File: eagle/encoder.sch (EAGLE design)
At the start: 22 parts, among them IC1 LM339D, J1 SPI, U1 MCP42XXX, U2 ATMEGA328P

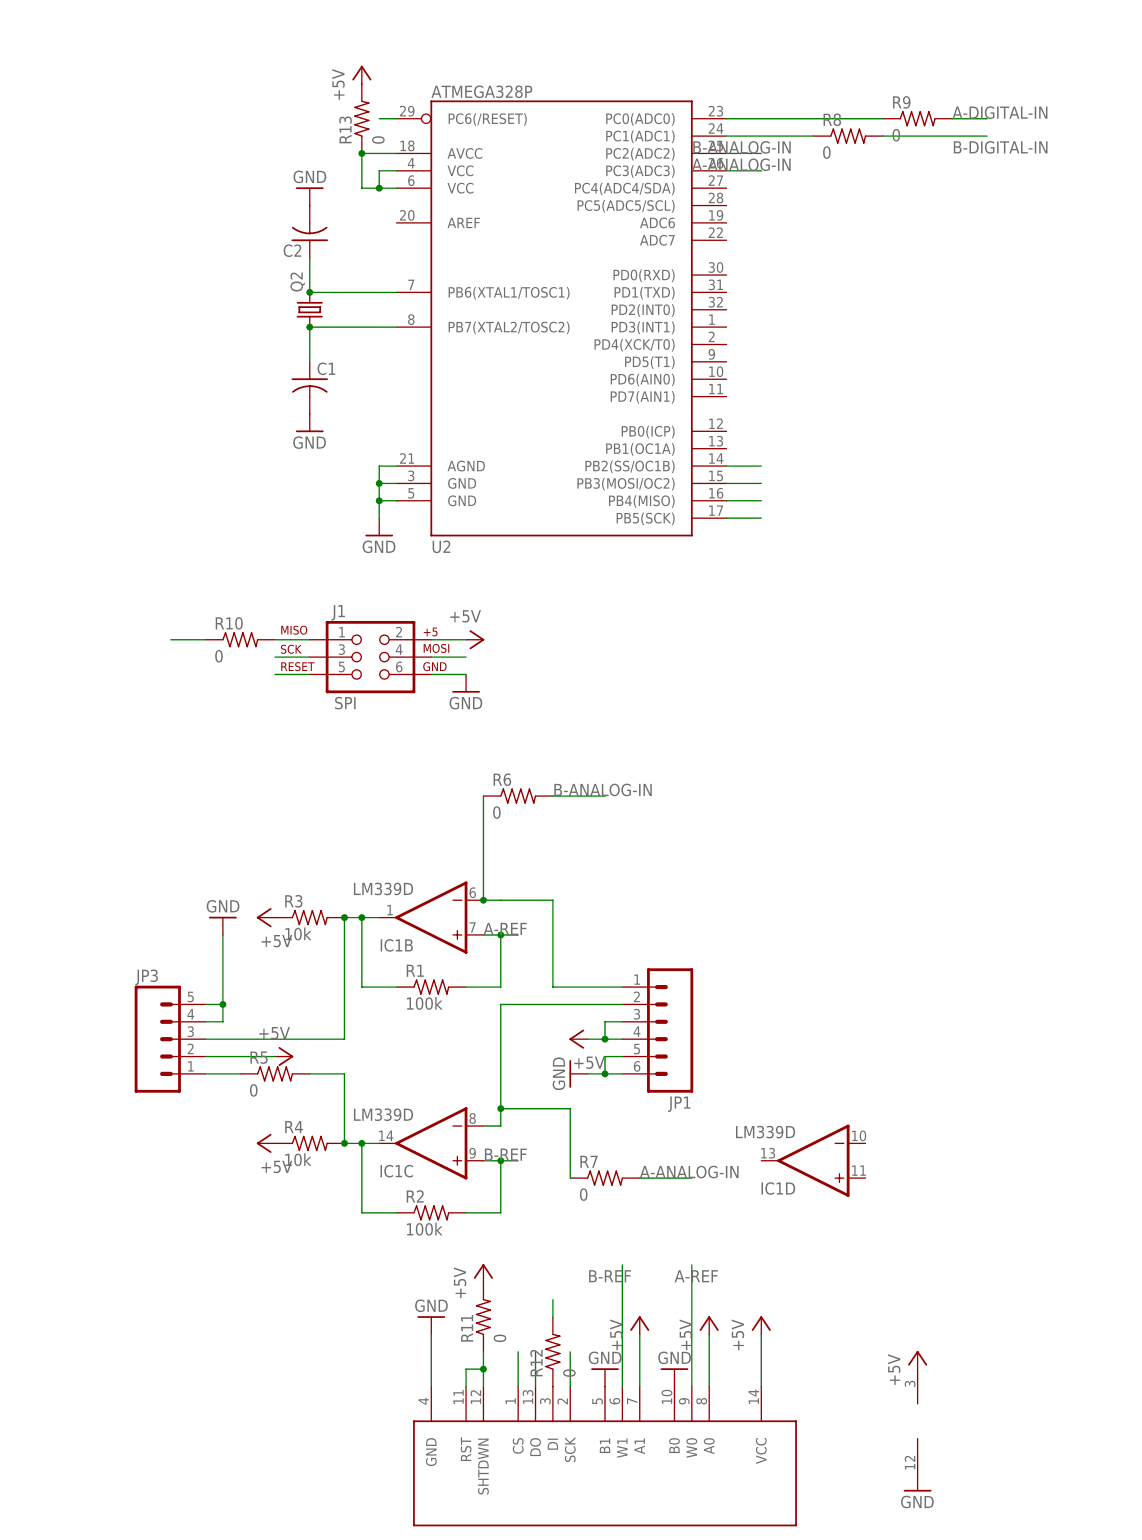
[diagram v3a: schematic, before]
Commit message: Added I2C and power connections.
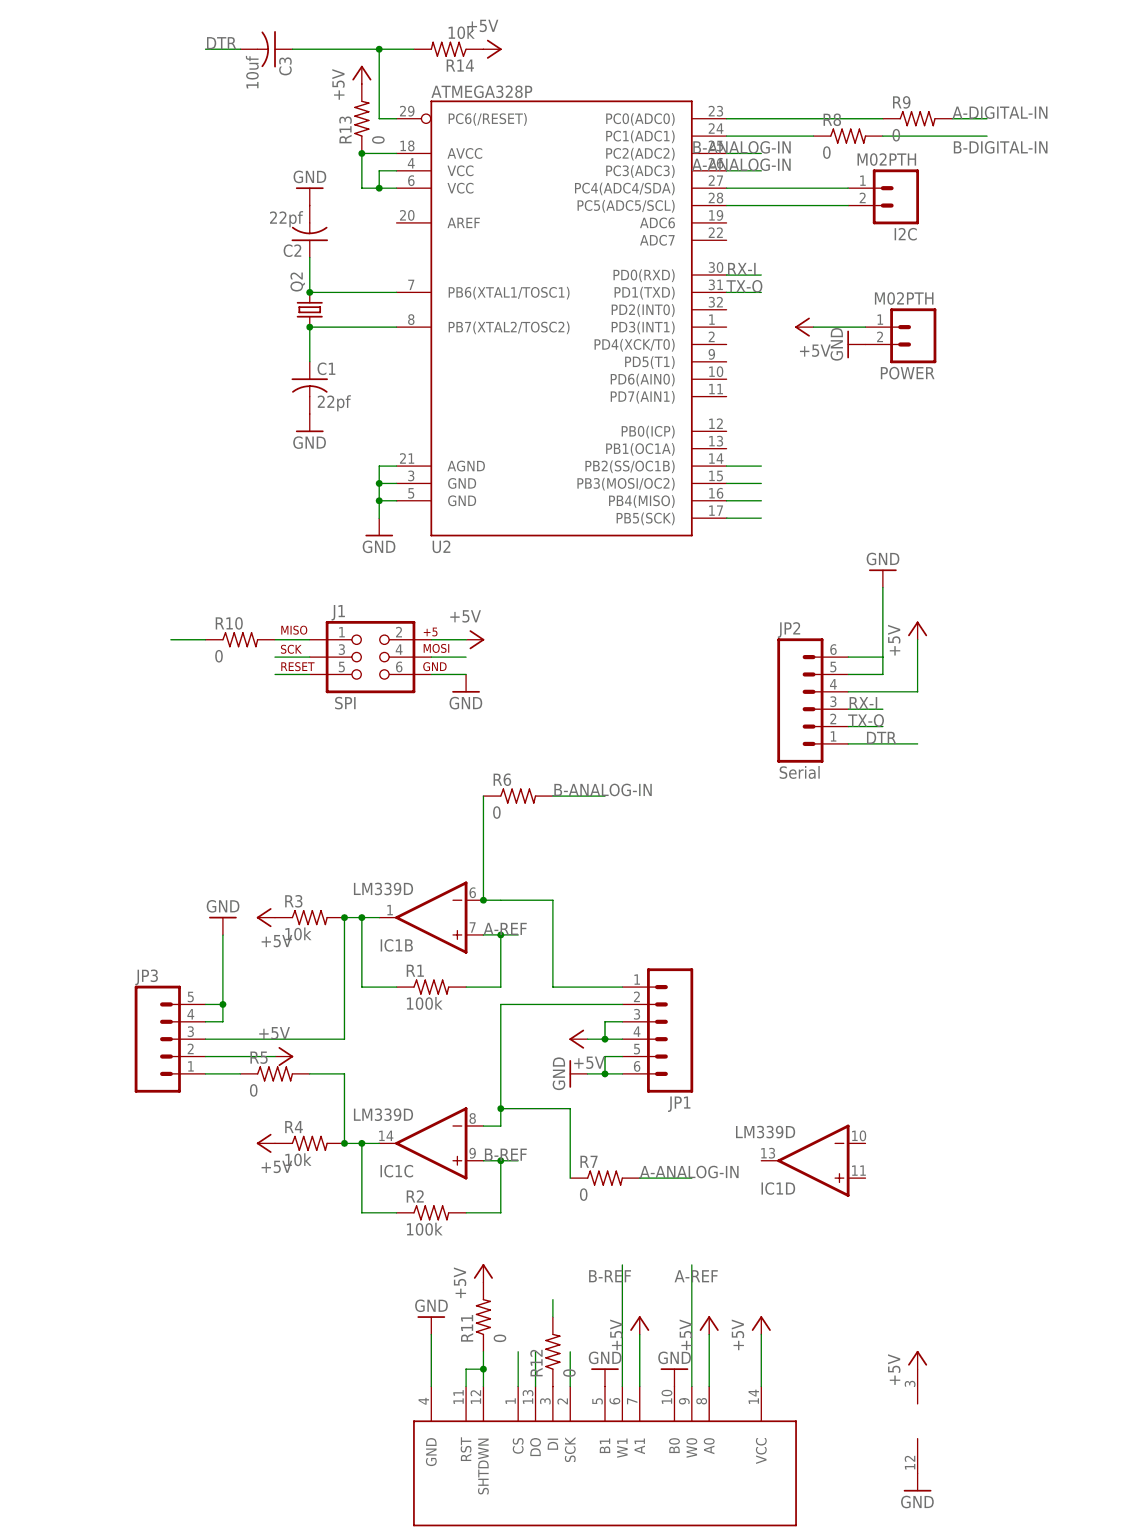
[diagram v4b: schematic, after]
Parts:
- added C3: 10uf, resistor:C-USC1206
- added I2C, POWER: M02PTH, SparkFun-Connectors:M02PTH
- added JP2: Serial, SparkFun-Connectors:M06SIP
- added R14: 10k, resistor:R-US_R1206
- C1, C2: value (none) -> 22pf
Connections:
- new net DTR: C3.2, JP2.1
- new net N$12: I2C.1, U2.PC4(ADC4/SDA)
- new net N$13: I2C.2, U2.PC5(ADC5/SCL)
- new net RX-I: JP2.3, U2.PD0(RXD)
- new net TX-O: JP2.2, U2.PD1(TXD)
- net +5V: now also JP2.4, POWER.1, R14.1
- net GND: now also JP2.5, JP2.6, POWER.2
- net RESET: now also C3.1, R14.2
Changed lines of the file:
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@@
 <part name="P+12" library="supply1" deviceset="+5V" device=""/>
 <part name="Q2" library="crystal" deviceset="CRYSTAL" device="HC49UP"/>
-<part name="C1" library="resistor" deviceset="C-US" device="C1206"/>
-<part name="C2" library="resistor" deviceset="C-US" device="C1206"/>
+<part name="C1" library="resistor" deviceset="C-US" device="C1206" value="22pf"/>
+<part name="C2" library="resistor" deviceset="C-US" device="C1206" value="22pf"/>
 <part name="GND9" library="supply1" deviceset="GND" device=""/>
 <part name="GND10" library="supply1" deviceset="GND" device=""/>
+<part name="R14" library="resistor" deviceset="R-US_" device="R1206" value="10k"/>
+<part name="P+9" library="supply1" deviceset="+5V" device=""/>
+<part name="C3" library="resistor" deviceset="C-US" device="C1206" value="10uf"/>
+<part name="JP2" library="SparkFun-Connectors" deviceset="M06" device="SIP" value="Serial"/>
+<part name="GND11" library="supply1" deviceset="GND" device=""/>
+<part name="P+13" library="supply1" deviceset="+5V" device=""/>
+<part name="I2C" library="SparkFun-Connectors" deviceset="M02" device="PTH"/>
+<part name="POWER" library="SparkFun-Connectors" deviceset="M02" device="PTH"/>
+<part name="P+14" library="supply1" deviceset="+5V" device=""/>
+<part name="GND12" library="supply1" deviceset="GND" device=""/>
 </parts>
 <sheets>
@@
 <instance part="GND9" gate="1" x="35.56" y="165.1"/>
 <instance part="GND10" gate="1" x="35.56" y="200.66" rot="R180"/>
+<instance part="R14" gate="G$1" x="55.88" y="220.98" rot="R180"/>
+<instance part="P+9" gate="1" x="63.5" y="220.98" rot="R270"/>
+<instance part="C3" gate="G$1" x="30.48" y="220.98" rot="R270"/>
+<instance part="JP2" gate="G$1" x="109.22" y="124.46"/>
+<instance part="GND11" gate="1" x="119.38" y="144.78" rot="R180"/>
+<instance part="P+13" gate="1" x="124.46" y="137.16"/>
+<instance part="I2C" gate="G$1" x="121.92" y="200.66" rot="R180"/>
+<instance part="POWER" gate="G$1" x="124.46" y="180.34" rot="R180"/>
+<instance part="P+14" gate="1" x="106.68" y="180.34" rot="R90"/>
+<instance part="GND12" gate="1" x="114.3" y="177.8" rot="R270"/>
 </instances>
 <busses>
@@
 <pinref part="P+12" gate="1" pin="+5V"/>
 </segment>
+<segment>
+<pinref part="R14" gate="G$1" pin="1"/>
+<pinref part="P+9" gate="1" pin="+5V"/>
+</segment>
+<segment>
+<pinref part="JP2" gate="G$1" pin="4"/>
+<wire x1="114.3" y1="127" x2="124.46" y2="127" width="0.1524" layer="91"/>
+<wire x1="124.46" y1="127" x2="124.46" y2="134.62" width="0.1524" layer="91"/>
+<pinref part="P+13" gate="1" pin="+5V"/>
+</segment>
+<segment>
+<pinref part="POWER" gate="G$1" pin="1"/>
+<pinref part="P+14" gate="1" pin="+5V"/>
+<wire x1="109.22" y1="180.34" x2="116.84" y2="180.34" width="0.1524" layer="91"/>
+</segment>
 </net>
 <net name="GND" class="0">
@@
 <pinref part="GND10" gate="1" pin="GND"/>
 </segment>
+<segment>
+<pinref part="JP2" gate="G$1" pin="5"/>
+<wire x1="114.3" y1="129.54" x2="119.38" y2="129.54" width="0.1524" layer="91"/>
+<wire x1="119.38" y1="129.54" x2="119.38" y2="132.08" width="0.1524" layer="91"/>
+<pinref part="JP2" gate="G$1" pin="6"/>
+<wire x1="119.38" y1="132.08" x2="119.38" y2="142.24" width="0.1524" layer="91"/>
+<wire x1="114.3" y1="132.08" x2="119.38" y2="132.08" width="0.1524" layer="91"/>
+<pinref part="GND11" gate="1" pin="GND"/>
+</segment>
+<segment>
+<pinref part="POWER" gate="G$1" pin="2"/>
+<pinref part="GND12" gate="1" pin="GND"/>
+</segment>
 </net>
 <net name="B-REF" class="0">
@@
 <pinref part="U2" gate="G$1" pin="PC6(/RESET)"/>
 <wire x1="48.26" y1="210.82" x2="45.72" y2="210.82" width="0.1524" layer="91"/>
+<wire x1="45.72" y1="210.82" x2="45.72" y2="220.98" width="0.1524" layer="91"/>
+<wire x1="45.72" y1="220.98" x2="50.8" y2="220.98" width="0.1524" layer="91"/>
+<pinref part="R14" gate="G$1" pin="2"/>
+<wire x1="45.72" y1="220.98" x2="33.02" y2="220.98" width="0.1524" layer="91"/>
+<pinref part="C3" gate="G$1" pin="1"/>
+<junction x="45.72" y="220.98"/>
 </segment>
 <segment>
@@
 </segment>
 </net>
+<net name="DTR" class="0">
+<segment>
+<pinref part="C3" gate="G$1" pin="2"/>
+<wire x1="25.4" y1="220.98" x2="20.32" y2="220.98" width="0.1524" layer="91"/>
+<label x="20.32" y="220.98" size="1.778" layer="95"/>
+</segment>
+<segment>
+<wire x1="114.3" y1="119.38" x2="124.46" y2="119.38" width="0.1524" layer="91"/>
+<label x="116.84" y="119.38" size="1.778" layer="95"/>
+<pinref part="JP2" gate="G$1" pin="1"/>
+</segment>
+</net>
+<net name="RX-I" class="0">
+<segment>
+<pinref part="U2" gate="G$1" pin="PD0(RXD)"/>
+<wire x1="96.52" y1="187.96" x2="101.6" y2="187.96" width="0.1524" layer="91"/>
+<label x="96.52" y="187.96" size="1.778" layer="95"/>
+</segment>
+<segment>
+<wire x1="114.3" y1="124.46" x2="119.38" y2="124.46" width="0.1524" layer="91"/>
+<label x="114.3" y="124.46" size="1.778" layer="95"/>
+<pinref part="JP2" gate="G$1" pin="3"/>
+</segment>
+</net>
+<net name="TX-O" class="0">
+<segment>
+<pinref part="U2" gate="G$1" pin="PD1(TXD)"/>
+<wire x1="96.52" y1="185.42" x2="101.6" y2="185.42" width="0.1524" layer="91"/>
+<label x="96.52" y="185.42" size="1.778" layer="95"/>
+</segment>
+<segment>
+<wire x1="114.3" y1="121.92" x2="119.38" y2="121.92" width="0.1524" layer="91"/>
+<label x="114.3" y="121.92" size="1.778" layer="95"/>
+<pinref part="JP2" gate="G$1" pin="2"/>
+</segment>
+</net>
+<net name="N$12" class="0">
+<segment>
+<pinref part="U2" gate="G$1" pin="PC4(ADC4/SDA)"/>
+<wire x1="96.52" y1="200.66" x2="114.3" y2="200.66" width="0.1524" layer="91"/>
+<pinref part="I2C" gate="G$1" pin="1"/>
+</segment>
+</net>
+<net name="N$13" class="0">
+<segment>
+<pinref part="U2" gate="G$1" pin="PC5(ADC5/SCL)"/>
+<wire x1="96.52" y1="198.12" x2="114.3" y2="198.12" width="0.1524" layer="91"/>
+<pinref part="I2C" gate="G$1" pin="2"/>
+</segment>
+</net>

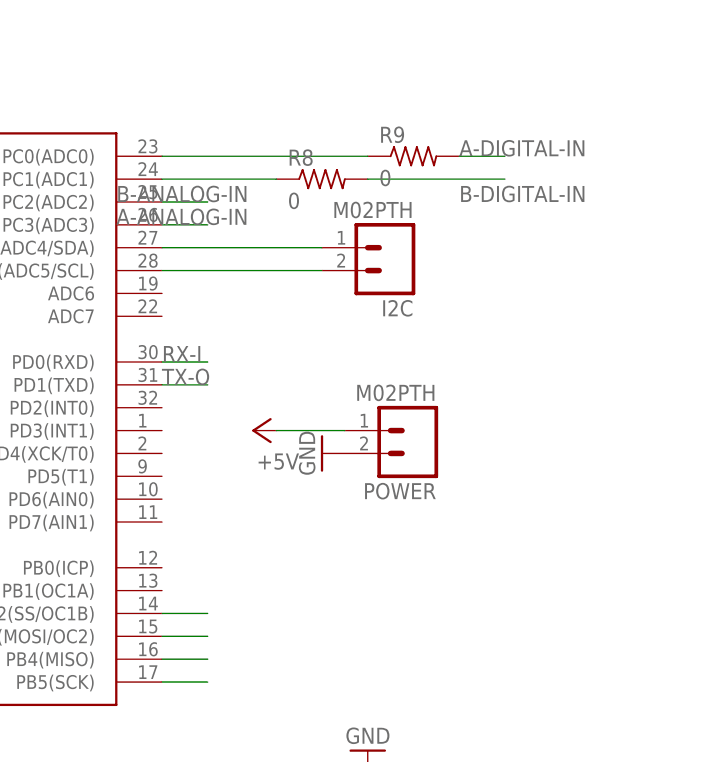
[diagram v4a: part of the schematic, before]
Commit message: Fixed an issue where the digital output channels were not connected to interrupts.
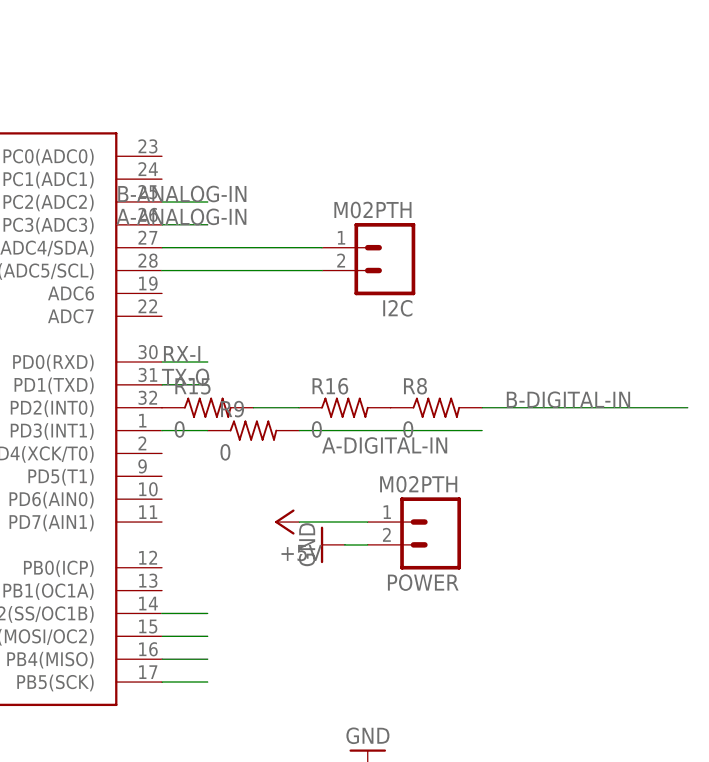
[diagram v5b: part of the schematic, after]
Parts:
- added R15, R16: 0, resistor:R-US_R1206
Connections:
- new net N$14: R15.2, R16.1
- new net N$15: R16.2, R8.1
- net N$6: now also R15.1, U2.PD2(INT0); no longer R8.1, U2.PC1(ADC1)
- net N$7: now also U2.PD3(INT1); no longer U2.PC0(ADC0)
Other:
- moved on the sheet: POWER, R8, R9
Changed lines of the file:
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@@
 <part name="P+14" library="supply1" deviceset="+5V" device=""/>
 <part name="GND12" library="supply1" deviceset="GND" device=""/>
+<part name="R15" library="resistor" deviceset="R-US_" device="R1206" value="0"/>
+<part name="R16" library="resistor" deviceset="R-US_" device="R1206" value="0"/>
 </parts>
 <sheets>
@@
 <instance part="R7" gate="G$1" x="78.74" y="55.88"/>
 <instance part="U2" gate="G$1" x="71.12" y="185.42"/>
-<instance part="R8" gate="G$1" x="114.3" y="208.28"/>
-<instance part="R9" gate="G$1" x="124.46" y="210.82"/>
+<instance part="R8" gate="G$1" x="127" y="182.88"/>
+<instance part="R9" gate="G$1" x="106.68" y="180.34"/>
 <instance part="R10" gate="G$1" x="25.4" y="134.62"/>
 <instance part="J1" gate="G$1" x="43.18" y="132.08"/>
@@
 <instance part="P+13" gate="1" x="124.46" y="137.16"/>
 <instance part="I2C" gate="G$1" x="121.92" y="200.66" rot="R180"/>
-<instance part="POWER" gate="G$1" x="124.46" y="180.34" rot="R180"/>
-<instance part="P+14" gate="1" x="106.68" y="180.34" rot="R90"/>
-<instance part="GND12" gate="1" x="114.3" y="177.8" rot="R270"/>
+<instance part="POWER" gate="G$1" x="127" y="170.18" rot="R180"/>
+<instance part="P+14" gate="1" x="109.22" y="170.18" rot="R90"/>
+<instance part="GND12" gate="1" x="114.3" y="167.64" rot="R270"/>
+<instance part="R15" gate="G$1" x="101.6" y="182.88"/>
+<instance part="R16" gate="G$1" x="116.84" y="182.88"/>
 </instances>
 <busses>
@@
 <pinref part="POWER" gate="G$1" pin="1"/>
 <pinref part="P+14" gate="1" pin="+5V"/>
-<wire x1="109.22" y1="180.34" x2="116.84" y2="180.34" width="0.1524" layer="91"/>
+<wire x1="111.76" y1="170.18" x2="119.38" y2="170.18" width="0.1524" layer="91"/>
 </segment>
 </net>
@@
 <pinref part="POWER" gate="G$1" pin="2"/>
 <pinref part="GND12" gate="1" pin="GND"/>
+<wire x1="119.38" y1="167.64" x2="116.84" y2="167.64" width="0.1524" layer="91"/>
 </segment>
 </net>
@@
 </segment>
 </net>
-<net name="N$6" class="0">
-<segment>
-<pinref part="U2" gate="G$1" pin="PC1(ADC1)"/>
-<pinref part="R8" gate="G$1" pin="1"/>
-<wire x1="109.22" y1="208.28" x2="96.52" y2="208.28" width="0.1524" layer="91"/>
-</segment>
-</net>
-<net name="N$7" class="0">
-<segment>
-<pinref part="U2" gate="G$1" pin="PC0(ADC0)"/>
-<pinref part="R9" gate="G$1" pin="1"/>
-<wire x1="119.38" y1="210.82" x2="96.52" y2="210.82" width="0.1524" layer="91"/>
-</segment>
-</net>
 <net name="A-DIGITAL-IN" class="0">
 <segment>
 <pinref part="R9" gate="G$1" pin="2"/>
-<wire x1="129.54" y1="210.82" x2="134.62" y2="210.82" width="0.1524" layer="91"/>
-<label x="129.54" y="210.82" size="1.778" layer="95"/>
+<wire x1="111.76" y1="180.34" x2="132.08" y2="180.34" width="0.1524" layer="91"/>
+<label x="114.3" y="177.8" size="1.778" layer="95"/>
 </segment>
 <segment>
@@
 <segment>
 <pinref part="R8" gate="G$1" pin="2"/>
-<wire x1="119.38" y1="208.28" x2="134.62" y2="208.28" width="0.1524" layer="91"/>
-<label x="129.54" y="205.74" size="1.778" layer="95"/>
+<wire x1="132.08" y1="182.88" x2="154.94" y2="182.88" width="0.1524" layer="91"/>
+<label x="134.62" y="182.88" size="1.778" layer="95"/>
 </segment>
 <segment>
@@
 </segment>
 </net>
+<net name="N$7" class="0">
+<segment>
+<pinref part="U2" gate="G$1" pin="PD3(INT1)"/>
+<pinref part="R9" gate="G$1" pin="1"/>
+<wire x1="101.6" y1="180.34" x2="96.52" y2="180.34" width="0.1524" layer="91"/>
+</segment>
+</net>
+<net name="N$14" class="0">
+<segment>
+<pinref part="R16" gate="G$1" pin="1"/>
+<pinref part="R15" gate="G$1" pin="2"/>
+<wire x1="106.68" y1="182.88" x2="111.76" y2="182.88" width="0.1524" layer="91"/>
+</segment>
+</net>
+<net name="N$6" class="0">
+<segment>
+<pinref part="U2" gate="G$1" pin="PD2(INT0)"/>
+<pinref part="R15" gate="G$1" pin="1"/>
+</segment>
+</net>
+<net name="N$15" class="0">
+<segment>
+<pinref part="R8" gate="G$1" pin="1"/>
+<pinref part="R16" gate="G$1" pin="2"/>
+</segment>
+</net>
